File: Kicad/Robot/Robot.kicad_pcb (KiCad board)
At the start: 2 copper layers, 159 x 76.9 mm, 49 parts, among them J1 PositiveBus, J10 LORA, J11 RELAY HEADER, J12 X8R HEADER, J13 SENSOR 1, J14 SENSOR 2, J15 SENSOR 3, J16 SENSOR 4, J2 NegativeBus, J3 PIN HEADER DE0-NANO POWER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

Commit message: layout complete for review
layout complete for review
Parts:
- J8: value BreakoutHeader -> Conn_01x05; footprint Robot:PinHeader_1x06_P2.54mm_Vertical -> Robot:PinHeader_1x05_P2.54mm_Vertical
- moved J10 70.5 mm to (26.2, 56.2), turned to 180 degrees
- moved J8 13.9 mm to (24.8, 41.5), turned to 270 degrees
- moved J4 7.65 mm to (59.2, -6.50)
- moved J5 7.58 mm to (41.4, -6.50)
- moved C3 5.40 mm to (-1.70, 36.4), turned to 90 degrees
- moved R2 4.93 mm to (5.07, 6.50), turned to 270 degrees
- moved R7 3.92 mm to (74.9, 52.4), turned to 270 degrees
- moved J3 3.87 mm to (-1.01, 39.4), turned to 0 degrees
- moved JP3 3.57 mm to (-37.6, 4.65), turned to 180 degrees
- moved R1 2.59 mm to (2.53, 6.51), turned to 270 degrees
- moved C2 2.50 mm to (-1.40, 54.5)
- moved C12 2.38 mm to (51.7, 17.0)
- moved R5 2.25 mm to (75.0, 10.2)
- moved C11 1.70 mm to (67.7, 33.0)
- moved J1 1.39 mm to (-56.0, 1.30)
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- renumbered POWER_INPUT1 to PI1
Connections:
- J9 pad 6: VCC3P3 -> Net-(J9-Pad6)
- JP1 pad 32: Net-(JP1-Pad32) -> Net-(J4-Pad3)
- JP1 pad 34: Net-(JP1-Pad34) -> Net-(J4-Pad2)
- JP1 pad 36: Net-(JP1-Pad36) -> Net-(J4-Pad1)
- JP1 pad 38: RX -> Net-(JP1-Pad38)
- JP1 pad 40: TX -> Net-(JP1-Pad40)
- JP1 pad 6: RST -> CS
- JP1 pad 8: CS -> RST
- JP2 pad 29: VCC3P3 -> Net-(J9-Pad6)
- JP2 pad 30: Net-(J8-Pad6) -> Net-(JP2-Pad30)
- JP2 pad 31: Net-(JP2-Pad31) -> Net-(J8-Pad1)
- JP2 pad 32: Net-(J8-Pad5) -> Net-(JP2-Pad32)
- JP2 pad 33: Net-(JP2-Pad33) -> Net-(J8-Pad2)
- JP2 pad 34: Net-(J8-Pad4) -> Net-(JP2-Pad34)
- JP2 pad 35: Net-(JP2-Pad35) -> Net-(J8-Pad3)
- JP2 pad 36: Net-(J8-Pad3) -> Net-(JP2-Pad36)
- JP2 pad 37: Net-(JP2-Pad37) -> Net-(J8-Pad4)
- JP2 pad 38: Net-(J8-Pad2) -> RX
- JP2 pad 39: Net-(JP2-Pad39) -> Net-(J8-Pad5)
- JP2 pad 40: Net-(J8-Pad1) -> TX
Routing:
- net GND: track 0.00 -> 491.5 mm
- net Net-(J1-Pad1): track 0.00 -> 206.5 mm
- net Net-(J2-Pad1): track 0.00 -> 197.5 mm
- net PWR_IND_SENSOR: track 0.00 -> 180.3 mm
- net VCC3P3: track 0.00 -> 174.3 mm
- net PWR_8CH_RLY: track 0.00 -> 140.9 mm
- net PWR_8XR: track 0.00 -> 103.5 mm
- net RST: track 0.00 -> 41.1 mm
- net Net-(JP2-Pad4): track 0.00 -> 40.2 mm
- net Net-(JP2-Pad17): track 0.00 -> 38.6 mm
- net SENSOR3: track 0.00 -> 37.5 mm
- net Net-(JP2-Pad15): track 0.00 -> 36.0 mm
- net Net-(JP1-Pad31): track 0.00 -> 34.3 mm
- net SENSOR4: track 0.00 -> 33.8 mm
- net Net-(JP2-Pad2): track 0.00 -> 33.6 mm
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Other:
- board size 159 x 76.9 mm -> 159 x 78.5 mm
- board text added: "+"
- board text added: "-"
- board text added: "2019"
- board text added: "BAT +"
- board text added: "BAT -"
- board text added: "GND"
- board text added: "IN"
- board text added: "LIGHTS +"
- board text added: "LIGHTS -"
- board text added: "MTR 1"
- board text added: "MTR 2"
- board text added: "RX"
- board text added: "TX"
- board text added: "Terrafirma Technology, Inc"

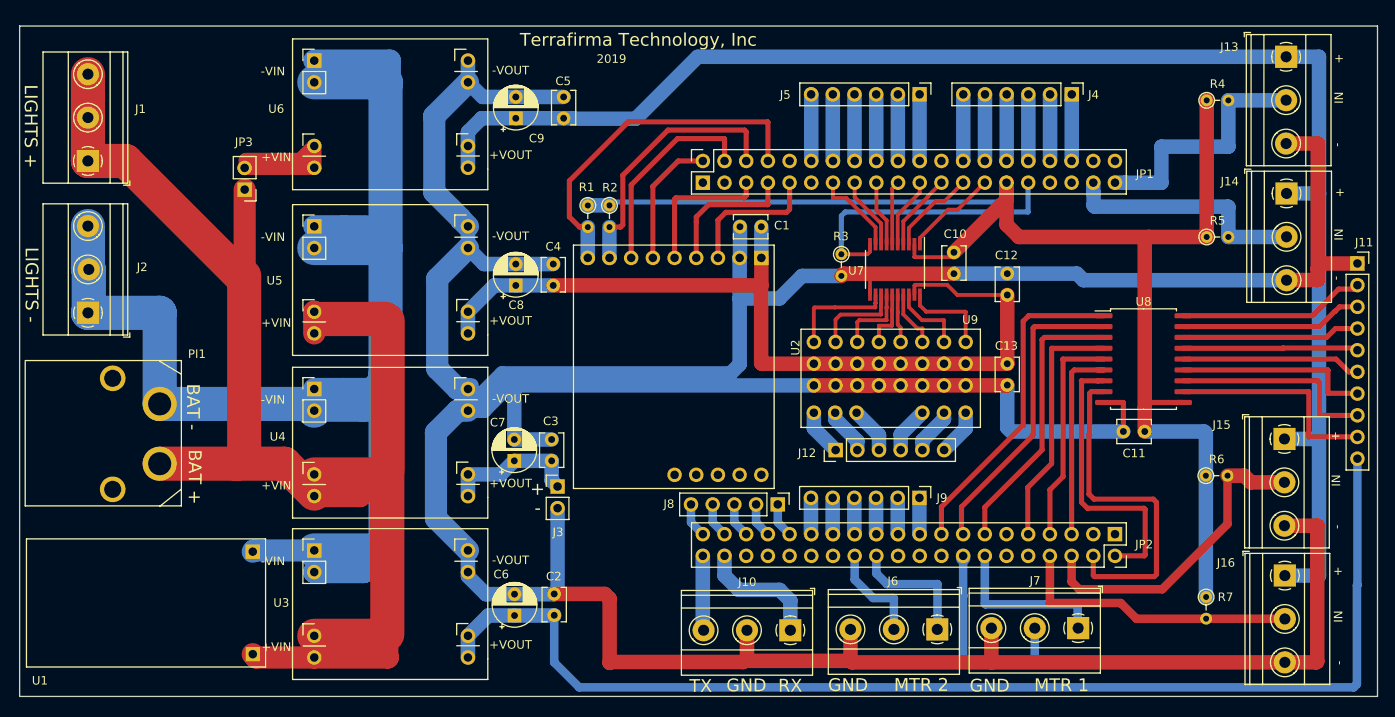
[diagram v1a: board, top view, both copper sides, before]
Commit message: added mounting holes
add mounting holes
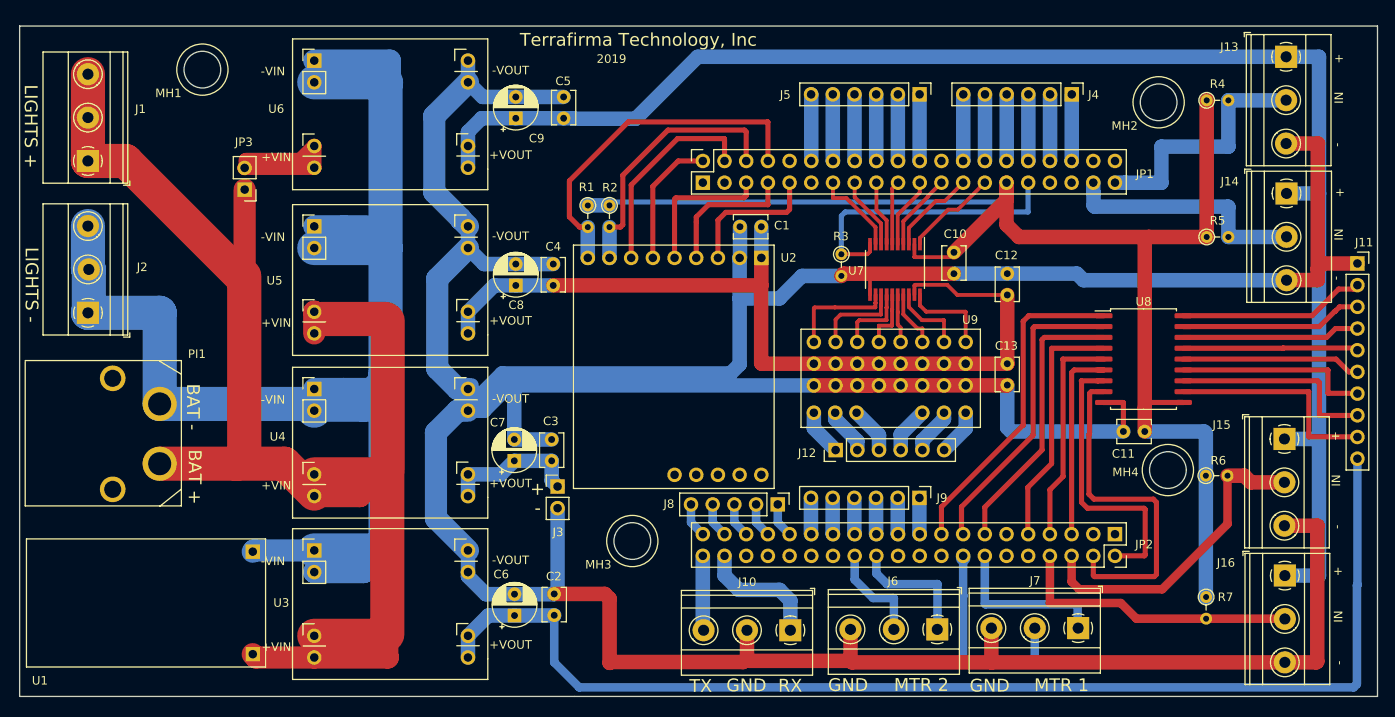
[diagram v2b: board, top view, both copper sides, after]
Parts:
- added MH1: MountingHole_4.3mm_M4, Robot:MountingHole_4.3mm_M4, F.Cu at (-42.6, -9.40)
- added MH2: MountingHole_4.3mm_M4, Robot:MountingHole_4.3mm_M4, F.Cu at (69.4, -5.57)
- added MH3: MountingHole_4.3mm_M4, Robot:MountingHole_4.3mm_M4, F.Cu at (7.74, 45.8)
- added MH4: MountingHole_4.3mm_M4, Robot:MountingHole_4.3mm_M4, F.Cu at (70.5, 37.5)
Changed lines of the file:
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@@
     (tracks 628)
     (zones 0)
-    (modules 49)
+    (modules 53)
     (nets 116)
   )
@@
   )
   (setup
-    (last_trace_width 1.7)
+    (last_trace_width 0.25)
     (user_trace_width 0.45)
     (user_trace_width 0.6)
@@
     (add_net VCC3P3)
   )
+  (module Robot:MountingHole_4.3mm_M4 (layer F.Cu)
+    (at 7.74192 45.80382)
+    (descr "Mounting Hole 4.3mm, no annular, M4")
+    (tags "mounting hole 4.3mm no annular m4")
+    (attr virtual)
+    (fp_text reference MH3 (at -3.98018 2.75844) (layer F.SilkS)
+      (effects (font (size 1 1) (thickness 0.15)))
+    )
+    (fp_text value MountingHole_4.3mm_M4 (at 0.23876 6.60146) (layer F.Fab)
+      (effects (font (size 1 1) (thickness 0.15)))
+    )
+    (fp_text user %R (at 0.3 0) (layer F.Fab)
+      (effects (font (size 1 1) (thickness 0.15)))
+    )
+    (fp_circle (center 0 0) (end 3 0) (layer F.SilkS) (width 0.12))
+    (pad "" np_thru_hole circle (at 0 0) (size 4.3 4.3) (drill 4.3) (layers *.Cu *.Mask))
+  )
+  (module Robot:MountingHole_4.3mm_M4 (layer F.Cu)
+    (at -42.59834 -9.39546)
+    (descr "Mounting Hole 4.3mm, no annular, M4")
+    (tags "mounting hole 4.3mm no annular m4")
+    (attr virtual)
+    (fp_text reference MH1 (at -3.98018 2.75844) (layer F.SilkS)
+      (effects (font (size 1 1) (thickness 0.15)))
+    )
+    (fp_text value MountingHole_4.3mm_M4 (at 0.23876 6.60146) (layer F.Fab)
+      (effects (font (size 1 1) (thickness 0.15)))
+    )
+    (fp_circle (center 0 0) (end 3 0) (layer F.SilkS) (width 0.12))
+    (fp_text user %R (at 0.3 0) (layer F.Fab)
+      (effects (font (size 1 1) (thickness 0.15)))
+    )
+    (pad "" np_thru_hole circle (at 0 0) (size 4.3 4.3) (drill 4.3) (layers *.Cu *.Mask))
+  )
+  (module Robot:MountingHole_4.3mm_M4 (layer F.Cu)
+    (at 69.37248 -5.57022)
+    (descr "Mounting Hole 4.3mm, no annular, M4")
+    (tags "mounting hole 4.3mm no annular m4")
+    (attr virtual)
+    (fp_text reference MH2 (at -3.98018 2.75844) (layer F.SilkS)
+      (effects (font (size 1 1) (thickness 0.15)))
+    )
+    (fp_text value MountingHole_4.3mm_M4 (at 0.23876 6.60146) (layer F.Fab)
+      (effects (font (size 1 1) (thickness 0.15)))
+    )
+    (fp_text user %R (at 0.3 0) (layer F.Fab)
+      (effects (font (size 1 1) (thickness 0.15)))
+    )
+    (fp_circle (center 0 0) (end 3 0) (layer F.SilkS) (width 0.12))
+    (pad "" np_thru_hole circle (at 0 0) (size 4.3 4.3) (drill 4.3) (layers *.Cu *.Mask))
+  )
+  (module Robot:MountingHole_4.3mm_M4 (layer F.Cu)
+    (at 70.45706 37.49294)
+    (descr "Mounting Hole 4.3mm, no annular, M4")
+    (tags "mounting hole 4.3mm no annular m4")
+    (attr virtual)
+    (fp_text reference MH4 (at -4.96316 0.25146) (layer F.SilkS)
+      (effects (font (size 1 1) (thickness 0.15)))
+    )
+    (fp_text value MountingHole_4.3mm_M4 (at 0.23876 6.60146) (layer F.Fab)
+      (effects (font (size 1 1) (thickness 0.15)))
+    )
+    (fp_circle (center 0 0) (end 3 0) (layer F.SilkS) (width 0.12))
+    (fp_text user %R (at 0.3 0) (layer F.Fab)
+      (effects (font (size 1 1) (thickness 0.15)))
+    )
+    (pad "" np_thru_hole circle (at 0 0) (size 4.3 4.3) (drill 4.3) (layers *.Cu *.Mask))
+  )
   (module Robot:RFM9X (layer F.Cu)
     (at 22.85 12.65 270)
-    (fp_text reference U2 (at 10.5 -4 90) (layer F.SilkS)
+    (fp_text reference U2 (at -0.01604 -3.19008 180) (layer F.SilkS)
       (effects (font (size 1 1) (thickness 0.15)))
     )
@@
     (descr "Resistor, Axial_DIN0204 series, Axial, Vertical, pin pitch=2.54mm, 0.167W, length*diameter=3.6*1.6mm^2, http://cdn-reichelt.de/documents/datenblatt/B400/1_4W%23YAG.pdf")
     (tags "Resistor Axial_DIN0204 series Axial Vertical pin pitch 2.54mm 0.167W length 3.6mm diameter 1.6mm")
-    (fp_text reference R6 (at 1.27 -1.92) (layer F.SilkS)
+    (fp_text reference R6 (at 1.4651 -1.76704) (layer F.SilkS)
       (effects (font (size 1 1) (thickness 0.15)))
     )
@@
     (descr "C, Disc series, Radial, pin pitch=2.50mm, , diameter*width=3.8*2.6mm^2, Capacitor, http://www.vishay.com/docs/45233/krseries.pdf")
     (tags "C Disc series Radial pin pitch 2.50mm  diameter 3.8mm width 2.6mm Capacitor")
-    (fp_text reference C11 (at 1.25 -2.55) (layer F.SilkS)
-      (effects (font (size 1 1) (thickness 0.15)))
-    )
+    (fp_text reference C11 (at 2.5019 -2.6035) (layer F.SilkS)
+      (effects (font (size 1 1) (thickness 0.15)))
+    )

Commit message: fixed fpga power input and jp2 header, usb pad  positions, added some more mounting holes
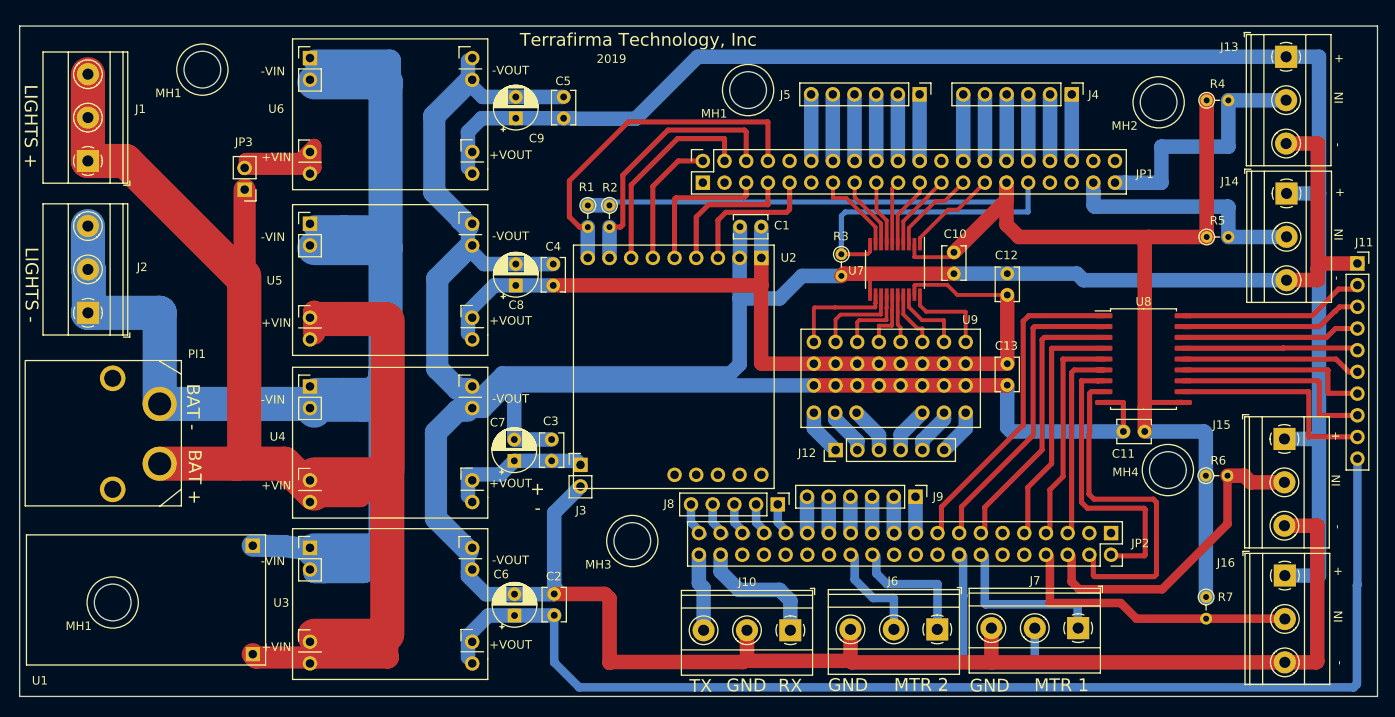
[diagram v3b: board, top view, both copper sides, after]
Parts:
- added MH1: MountingHole_4.3mm_M4, Robot:MountingHole_4.3mm_M4, F.Cu at (21.3, -7.00)
- added MH1: MountingHole_4.3mm_M4, Robot:MountingHole_4.3mm_M4, F.Cu at (-53.1, 53.0)
- moved J3 3.69 mm to (1.67, 36.9)
- moved JP2 0.48 mm to (63.8, 44.9)
- moved J9 0.48 mm to (40.9, 40.6)
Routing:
- net GND: track 491.5 -> 495.7 mm
